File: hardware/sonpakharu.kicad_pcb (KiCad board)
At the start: 2 copper layers, 51.3 x 71.1 mm, 60 parts, among them IC1 ESP32-S3-WROOM-1U-N4, J1 ADC1, J10 EXT2, J12 BATT, J13 EXT7, J14 PWR, J15 EXT8, J16 485, J17 ESP PRG, J3 ADC2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

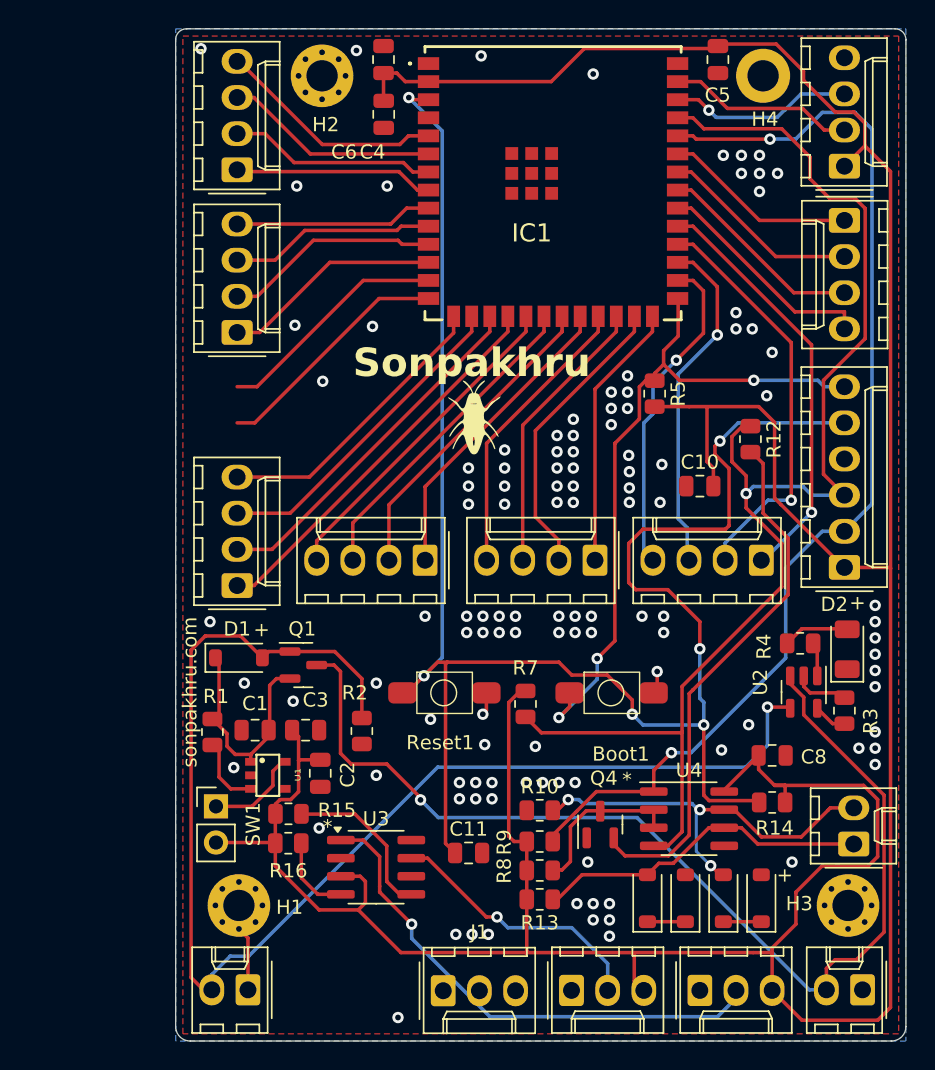
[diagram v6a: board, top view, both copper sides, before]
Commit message: rectified labels, all routing done
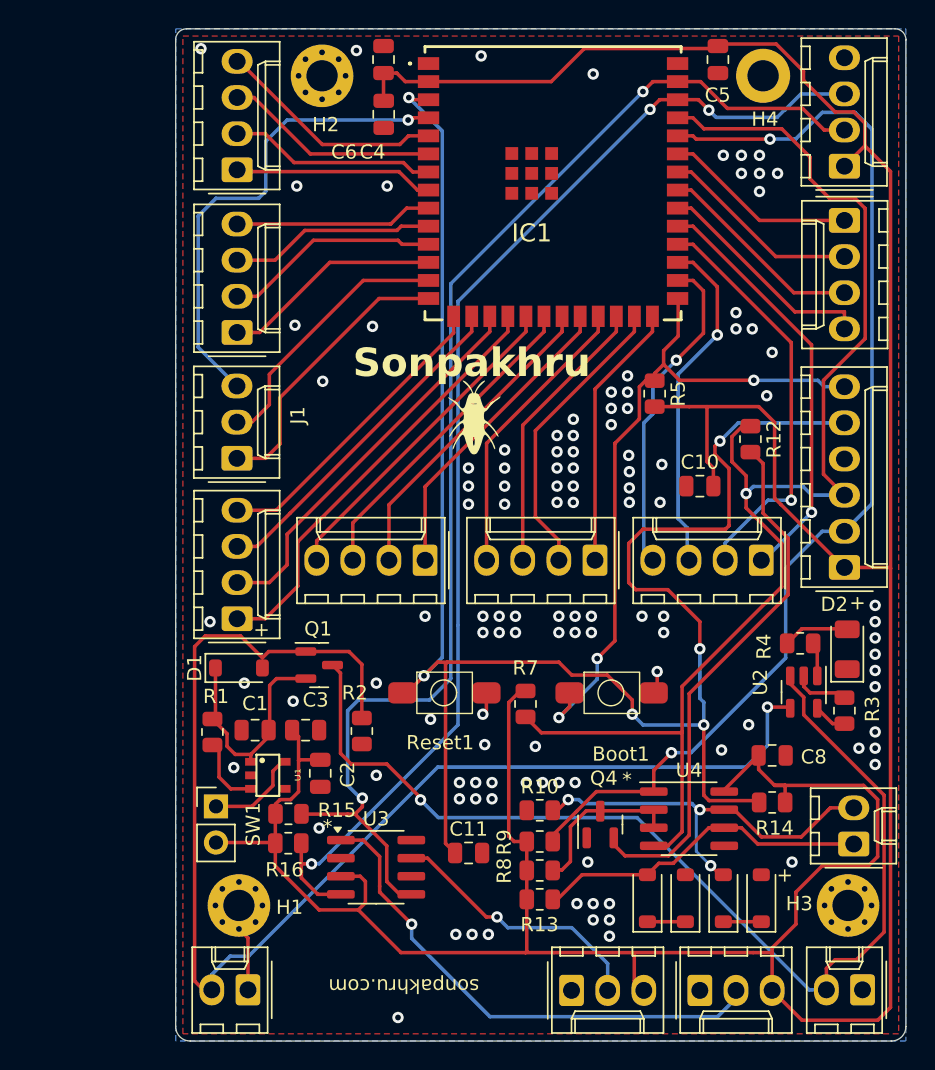
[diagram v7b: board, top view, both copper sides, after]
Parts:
- moved J1 40.1 mm to (110.2, 67.8), turned to 90 degrees
- moved J5 2.33 mm to (110.2, 79.0)
- moved Q1 1.11 mm to (116.0, 82.3)
- moved D1 0.71 mm to (110.4, 82.5)
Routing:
- net /SDA: track 18.6 -> 84.8 mm, vias 1 -> 3
- net /SCL: track 24.7 -> 90.6 mm, vias 0 -> 2
- net /IO4: track 0.00 -> 34.4 mm, vias 0 -> 1
- net /IO20: track 17.1 -> 20.0 mm
- net /IO10: track 27.5 -> 30.3 mm
- net /IO19: track 16.5 -> 18.8 mm
- net /IO9: track 25.2 -> 27.4 mm
- net +BATT: track 76.3 -> 75.2 mm
- net /IO3: track 20.6 -> 21.5 mm
- net /IO46: track 22.8 -> 23.8 mm
- net GND: vias 115 -> 113
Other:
- board text added: "35"
- board text added: "36"
- board text added: "37"
- board text added: "38"
- board text added: "39"
- board text added: "3V3"
- board text added: "40"
- board text added: "41"
- board text added: "42"
- board text added: "45"
- board text added: "46"
- board text added: "47"
- board text added: "48"
- board text added: "EN"
- board text added: "GND"
- board text added: "IO0"
- board text removed: "1"
- board text removed: "2"
- board text removed: "22"
- board text removed: "23"
- board text removed: "24"
- board text removed: "25"
- board text removed: "26"
- board text removed: "27"
- board text removed: "28"
- board text removed: "29"
- board text removed: "30"
- board text removed: "DT"
- board text removed: "RT"

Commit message: Fix: layout u[dated
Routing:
- net /IO20: track 20.0 -> 22.8 mm
- net /IO19: track 18.8 -> 20.5 mm
- net /IO16: track 13.9 -> 15.5 mm
- net GND: vias 113 -> 157
